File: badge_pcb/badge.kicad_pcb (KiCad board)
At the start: 2 copper layers, 67.5 x 82.8 mm, 6 parts

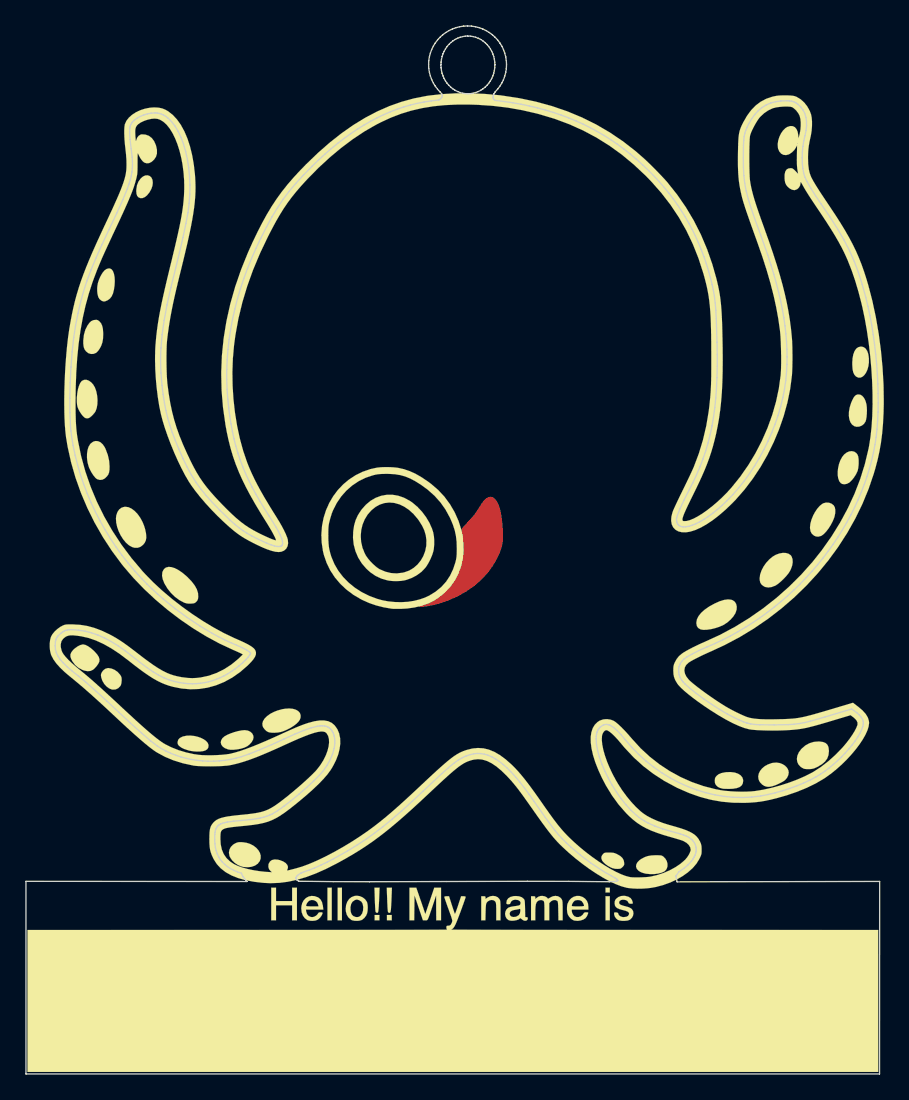
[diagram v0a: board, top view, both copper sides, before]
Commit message: Add dummy items on layers to get past PCBWay review.
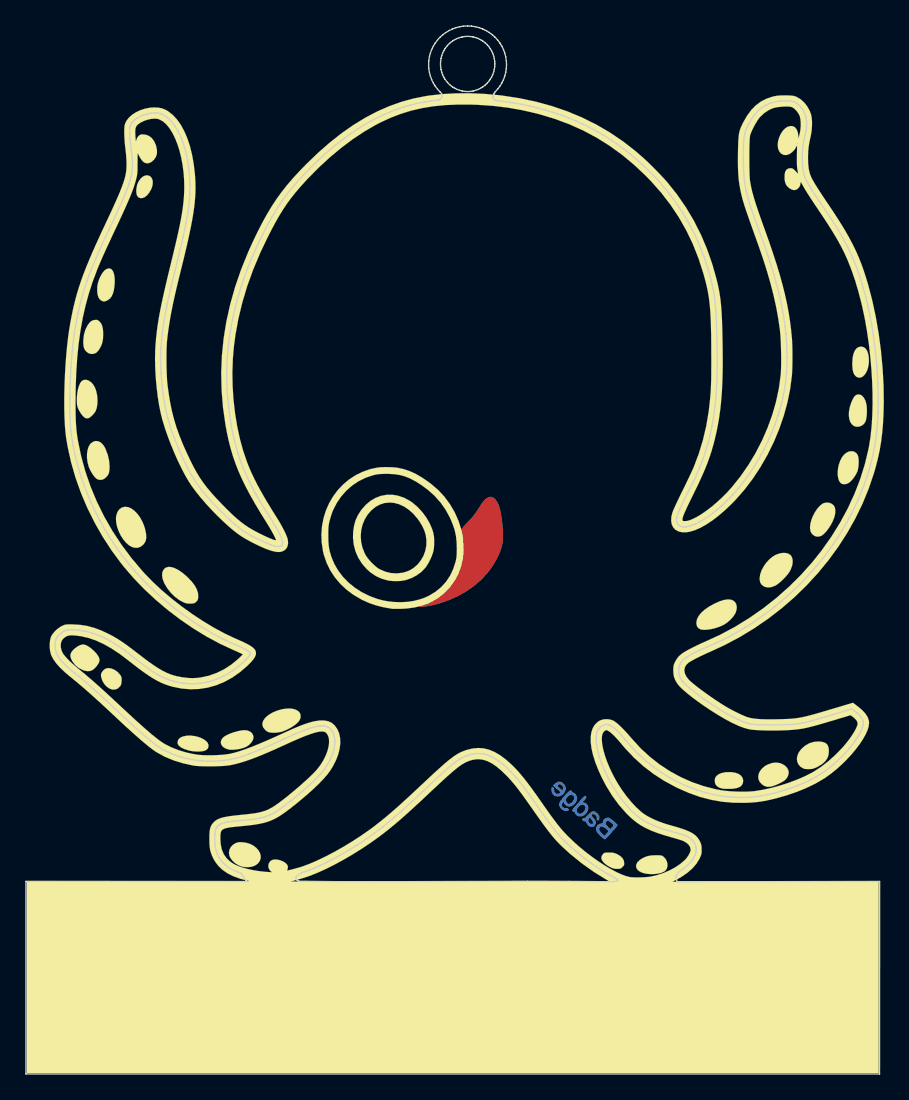
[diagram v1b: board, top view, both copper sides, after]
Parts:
- removed the G*** at (0.00, 0.00) (x6)
- added G*** (x6): LOGO, LOGO, F.Cu at (0.00, 0.00)
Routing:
- net (no net): vias 0 -> 1
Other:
- outline, holes or cut-outs redrawn
